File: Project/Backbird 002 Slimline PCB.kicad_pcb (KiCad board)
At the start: 2 copper layers, 10 parts

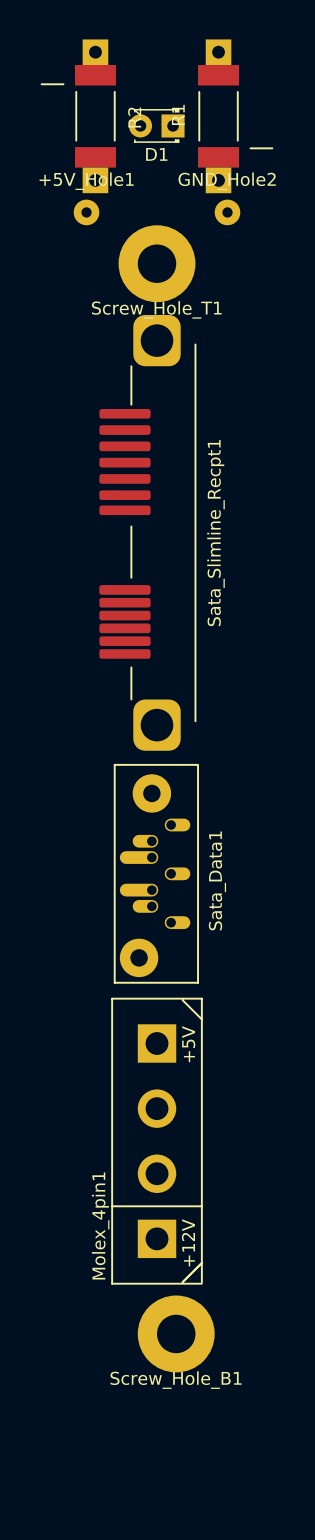
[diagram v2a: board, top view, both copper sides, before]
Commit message: Fixed Sata Slimline footprint to have pads instead of holes. Moved Sata receptacle to the back side of the PCB
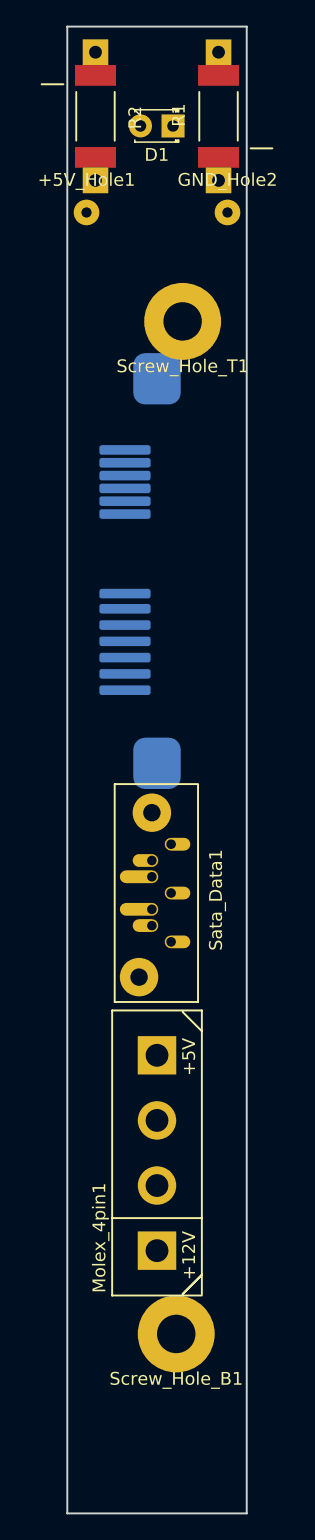
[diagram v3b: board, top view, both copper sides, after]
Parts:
- Sata_Slimline_Recpt1: moved to B.Cu
- moved Screw_Hole_T1 4.92 mm to (109.3, 53.5)
- moved Sata_Slimline_Recpt1 2.98 mm to (107.3, 73.0), turned to 270 degrees
- moved Sata_Data1 1.50 mm to (111.3, 106.5)
- moved Molex_4pin1 0.92 mm to (107.3, 118.4)
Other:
- board outline added: 14 x 116 mm
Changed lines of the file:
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@@
   (general
     (thickness 1.6)
-    (drawings 8)
+    (drawings 14)
     (tracks 0)
     (zones 0)
@@
     (add_net "Net-(Screw_Hole_T1-Pad1)")
   )
+  (module ProjectFootprints:SATA_SLIMLINE_RECPT_1735539-2 (layer B.Cu)
+    (at 107.3 72.96 270)
+    (attr smd)
+    (fp_text reference Sata_Slimline_Recpt1 (at 0 -4.5 270) (layer B.SilkS)
+      (effects (font (size 1 1) (thickness 0.15)) (justify mirror))
+    )
+    (fp_text value Conn_01x13 (at 0 8.08 270) (layer B.Fab)
+      (effects (font (size 1 1) (thickness 0.15)) (justify mirror))
+    )
+    (fp_line (start 10 2) (end 13 2) (layer B.SilkS) (width 0.15))
+    (fp_line (start -13 2) (end -10.5 2) (layer B.SilkS) (width 0.15))
+    (fp_line (start -3.5 2) (end 0.5 2) (layer B.SilkS) (width 0.15))
+    (fp_line (start 14.7 -3) (end -14.7 -3) (layer B.SilkS) (width 0.15))
+    (pad "" smd roundrect (at 15 0 270) (size 4 3.7) (layers B.Cu B.Paste B.Mask) (roundrect_rratio 0.25))
+    (pad "" smd roundrect (at -15 0 270) (size 4 3.7) (layers B.Cu B.Paste B.Mask) (roundrect_rratio 0.25))
+    (pad 7 smd roundrect (at 1.76 2.5 270) (size 0.75 4) (layers B.Cu B.Paste B.Mask) (roundrect_rratio 0.25)
+      (net 2 GND))
+    (pad 6 smd roundrect (at 2.94 2.5 270) (size 0.75 4) (layers B.Cu B.Paste B.Mask) (roundrect_rratio 0.25)
+      (net 5 B+))
+    (pad 5 smd roundrect (at 4.21 2.5 270) (size 0.75 4) (layers B.Cu B.Paste B.Mask) (roundrect_rratio 0.25)
+      (net 6 B-))
+    (pad 4 smd roundrect (at 5.48 2.5 270) (size 0.75 4) (layers B.Cu B.Paste B.Mask) (roundrect_rratio 0.25)
+      (net 2 GND))
+    (pad 3 smd roundrect (at 6.75 2.5 270) (size 0.75 4) (layers B.Cu B.Paste B.Mask) (roundrect_rratio 0.25)
+      (net 7 A-))
+    (pad 2 smd roundrect (at 8.02 2.5 270) (size 0.75 4) (layers B.Cu B.Paste B.Mask) (roundrect_rratio 0.25)
+      (net 8 A+))
+    (pad 1 smd roundrect (at 9.29 2.5 270) (size 0.75 4) (layers B.Cu B.Paste B.Mask) (roundrect_rratio 0.25)
+      (net 2 GND))
+    (pad 8 smd roundrect (at -4.45 2.5 270) (size 0.75 4) (layers B.Cu B.Paste B.Mask) (roundrect_rratio 0.25)
+      (net 10 "Net-(Sata_Slimline_Recpt1-Pad8)"))
+    (pad 9 smd roundrect (at -5.45 2.5 270) (size 0.75 4) (layers B.Cu B.Paste B.Mask) (roundrect_rratio 0.25)
+      (net 3 +5V))
+    (pad 10 smd roundrect (at -6.45 2.5 270) (size 0.75 4) (layers B.Cu B.Paste B.Mask) (roundrect_rratio 0.25)
+      (net 3 +5V))
+    (pad 11 smd roundrect (at -7.45 2.5 270) (size 0.75 4) (layers B.Cu B.Paste B.Mask) (roundrect_rratio 0.25)
+      (net 9 "Net-(Sata_Slimline_Recpt1-Pad11)"))
+    (pad 12 smd roundrect (at -8.45 2.5 270) (size 0.75 4) (layers B.Cu B.Paste B.Mask) (roundrect_rratio 0.25)
+      (net 2 GND))
+    (pad 13 smd roundrect (at -9.45 2.5 270) (size 0.75 4) (layers B.Cu B.Paste B.Mask) (roundrect_rratio 0.25)
+      (net 2 GND))
+  )
   (module Resistors_Universal:Resistor_SMD+THTuniversal_2512_RM10_HandSoldering (layer F.Cu)
     (at 102.5 37.4788 270)
@@
   )
   (module ProjectFootprints:SATA_DATA_678007005_CustomPad (layer F.Cu)
-    (at 111.3 104.98 90)
+    (at 111.3 106.48 90)
     (fp_text reference Sata_Data1 (at 7.86 0.6 90) (layer F.SilkS)
       (effects (font (size 1 1) (thickness 0.15)))
@@
   )
   (module ProjectFootprints:MOLEX_8981_0015244745 (layer F.Cu)
-    (at 107.3 117.44 90)
+    (at 107.3 118.36 90)
     (fp_text reference Molex_4pin1 (at -6.62 -4.5 90) (layer F.SilkS)
       (effects (font (size 1 1) (thickness 0.15)))
@@
       (net 1 "Net-(D1-Pad2)"))
   )
-  (module ProjectFootprints:SATA_SLIMLINE_RECPT_1735539-2 (layer F.Cu)
-    (at 107.3 69.98 90)
-    (attr smd)
-    (fp_text reference Sata_Slimline_Recpt1 (at 0 4.5 90) (layer F.SilkS)
-      (effects (font (size 1 1) (thickness 0.15)))
-    )
-    (fp_text value Conn_01x13 (at 0 -8.08 90) (layer F.Fab)
-      (effects (font (size 1 1) (thickness 0.15)))
-    )
-    (fp_line (start 10 -2) (end 13 -2) (layer F.SilkS) (width 0.15))
-    (fp_line (start -13 -2) (end -10.5 -2) (layer F.SilkS) (width 0.15))
-    (fp_line (start -3.5 -2) (end 0.5 -2) (layer F.SilkS) (width 0.15))
-    (fp_line (start 14.7 3) (end -14.7 3) (layer F.SilkS) (width 0.15))
-    (pad "" np_thru_hole roundrect (at 15 0 90) (size 4 3.7) (drill 2.54) (layers *.Cu *.Mask) (roundrect_rratio 0.25))
-    (pad "" np_thru_hole roundrect (at -15 0 90) (size 4 3.7) (drill 2.54) (layers *.Cu *.Mask) (roundrect_rratio 0.25))
-    (pad 7 smd roundrect (at 1.76 -2.5 90) (size 0.75 4) (layers F.Cu F.Paste F.Mask) (roundrect_rratio 0.25)
-      (net 2 GND))
-    (pad 6 smd roundrect (at 2.94 -2.5 90) (size 0.75 4) (layers F.Cu F.Paste F.Mask) (roundrect_rratio 0.25)
-      (net 5 B+))
-    (pad 5 smd roundrect (at 4.21 -2.5 90) (size 0.75 4) (layers F.Cu F.Paste F.Mask) (roundrect_rratio 0.25)
-      (net 6 B-))
-    (pad 4 smd roundrect (at 5.48 -2.5 90) (size 0.75 4) (layers F.Cu F.Paste F.Mask) (roundrect_rratio 0.25)
-      (net 2 GND))
-    (pad 3 smd roundrect (at 6.75 -2.5 90) (size 0.75 4) (layers F.Cu F.Paste F.Mask) (roundrect_rratio 0.25)
-      (net 7 A-))
-    (pad 2 smd roundrect (at 8.02 -2.5 90) (size 0.75 4) (layers F.Cu F.Paste F.Mask) (roundrect_rratio 0.25)
-      (net 8 A+))
-    (pad 1 smd roundrect (at 9.29 -2.5 90) (size 0.75 4) (layers F.Cu F.Paste F.Mask) (roundrect_rratio 0.25)
-      (net 2 GND))
-    (pad 8 smd roundrect (at -4.45 -2.5 90) (size 0.75 4) (layers F.Cu F.Paste F.Mask) (roundrect_rratio 0.25)
-      (net 10 "Net-(Sata_Slimline_Recpt1-Pad8)"))
-    (pad 9 smd roundrect (at -5.45 -2.5 90) (size 0.75 4) (layers F.Cu F.Paste F.Mask) (roundrect_rratio 0.25)
-      (net 3 +5V))
-    (pad 10 smd roundrect (at -6.45 -2.5 90) (size 0.75 4) (layers F.Cu F.Paste F.Mask) (roundrect_rratio 0.25)
-      (net 3 +5V))
-    (pad 11 smd roundrect (at -7.45 -2.5 90) (size 0.75 4) (layers F.Cu F.Paste F.Mask) (roundrect_rratio 0.25)
-      (net 9 "Net-(Sata_Slimline_Recpt1-Pad11)"))
-    (pad 12 smd roundrect (at -8.45 -2.5 90) (size 0.75 4) (layers F.Cu F.Paste F.Mask) (roundrect_rratio 0.25)
-      (net 2 GND))
-    (pad 13 smd roundrect (at -9.45 -2.5 90) (size 0.75 4) (layers F.Cu F.Paste F.Mask) (roundrect_rratio 0.25)
-      (net 2 GND))
-  )
   (module ProjectFootprints:Blackbird002_Slimline_PCB_Screw (layer F.Cu)
     (at 108.8 132.48)
@@
   )
   (module ProjectFootprints:Blackbird002_Slimline_PCB_Screw (layer F.Cu)
-    (at 107.3 48.98)
+    (at 109.3 53.48)
     (fp_text reference Screw_Hole_T1 (at 0 3.5) (layer F.SilkS)
       (effects (font (size 1 1) (thickness 0.15)))
@@
     (pad 1 thru_hole circle (at 0 0) (size 1.99898 1.99898) (drill 0.8001) (layers *.Cu *.Mask)
       (net 2 GND))
+  )
+  (gr_line (start 114.3 30.48) (end 114.3 146.48) (layer Edge.Cuts) (width 0.15))
+  (gr_line (start 100.3 30.48) (end 114.3 30.48) (layer Edge.Cuts) (width 0.15))
+  (gr_line (start 100.3 146.48) (end 100.3 30.48) (layer Edge.Cuts) (width 0.15))
+  (gr_line (start 114.3 146.48) (end 100.3 146.48) (layer Edge.Cuts) (width 0.15))
+  (dimension 4 (width 0.3) (layer F.SilkS)
+    (gr_text "4.000 mm" (at 112.3 25.38) (layer F.SilkS)
+      (effects (font (size 1.5 1.5) (thickness 0.3)))
+    )
+    (feature1 (pts (xy 110.3 28.98) (xy 110.3 26.893579)))
+    (feature2 (pts (xy 114.3 28.98) (xy 114.3 26.893579)))
+    (crossbar (pts (xy 114.3 27.48) (xy 110.3 27.48)))
+    (arrow1a (pts (xy 110.3 27.48) (xy 111.426504 26.893579)))
+    (arrow1b (pts (xy 110.3 27.48) (xy 111.426504 28.066421)))
+    (arrow2a (pts (xy 114.3 27.48) (xy 113.173496 26.893579)))
+    (arrow2b (pts (xy 114.3 27.48) (xy 113.173496 28.066421)))
+  )
+  (dimension 24.5 (width 0.3) (layer F.SilkS)
+    (gr_text "24.500 mm" (at 124.4 42.73 270) (layer F.SilkS)
+      (effects (font (size 1.5 1.5) (thickness 0.3)))
+    )
+    (feature1 (pts (xy 119.3 54.98) (xy 122.886421 54.98)))
+    (feature2 (pts (xy 119.3 30.48) (xy 122.886421 30.48)))
+    (crossbar (pts (xy 122.3 30.48) (xy 122.3 54.98)))
+    (arrow1a (pts (xy 122.3 54.98) (xy 121.713579 53.853496)))
+    (arrow1b (pts (xy 122.3 54.98) (xy 122.886421 53.853496)))
+    (arrow2a (pts (xy 122.3 30.48) (xy 121.713579 31.606504)))
+    (arrow2b (pts (xy 122.3 30.48) (xy 122.886421 31.606504)))
   )
   (dimension 8 (width 0.3) (layer Eco1.User)
@@
   )
   (dimension 116 (width 0.3) (layer Eco1.User)
-    (gr_text "116.000 mm" (at 126.4 88.48 270) (layer Eco1.User)
-      (effects (font (size 1.5 1.5) (thickness 0.3)))
-    )
-    (feature1 (pts (xy 119.3 146.48) (xy 124.886421 146.48)))
-    (feature2 (pts (xy 119.3 30.48) (xy 124.886421 30.48)))
-    (crossbar (pts (xy 124.3 30.48) (xy 124.3 146.48)))
-    (arrow1a (pts (xy 124.3 146.48) (xy 123.713579 145.353496)))
-    (arrow1b (pts (xy 124.3 146.48) (xy 124.886421 145.353496)))
-    (arrow2a (pts (xy 124.3 30.48) (xy 123.713579 31.606504)))
-    (arrow2b (pts (xy 124.3 30.48) (xy 124.886421 31.606504)))
+    (gr_text "116.000 mm" (at 131.4 88.48 270) (layer Eco1.User)
+      (effects (font (size 1.5 1.5) (thickness 0.3)))
+    )
+    (feature1 (pts (xy 124.3 146.48) (xy 129.886421 146.48)))
+    (feature2 (pts (xy 124.3 30.48) (xy 129.886421 30.48)))
+    (crossbar (pts (xy 129.3 30.48) (xy 129.3 146.48)))
+    (arrow1a (pts (xy 129.3 146.48) (xy 128.713579 145.353496)))
+    (arrow1b (pts (xy 129.3 146.48) (xy 129.886421 145.353496)))
+    (arrow2a (pts (xy 129.3 30.48) (xy 128.713579 31.606504)))
+    (arrow2b (pts (xy 129.3 30.48) (xy 129.886421 31.606504)))
   )
   (gr_line (start 114.3 30.48) (end 114.3 146.48) (layer Eco1.User) (width 0.2))

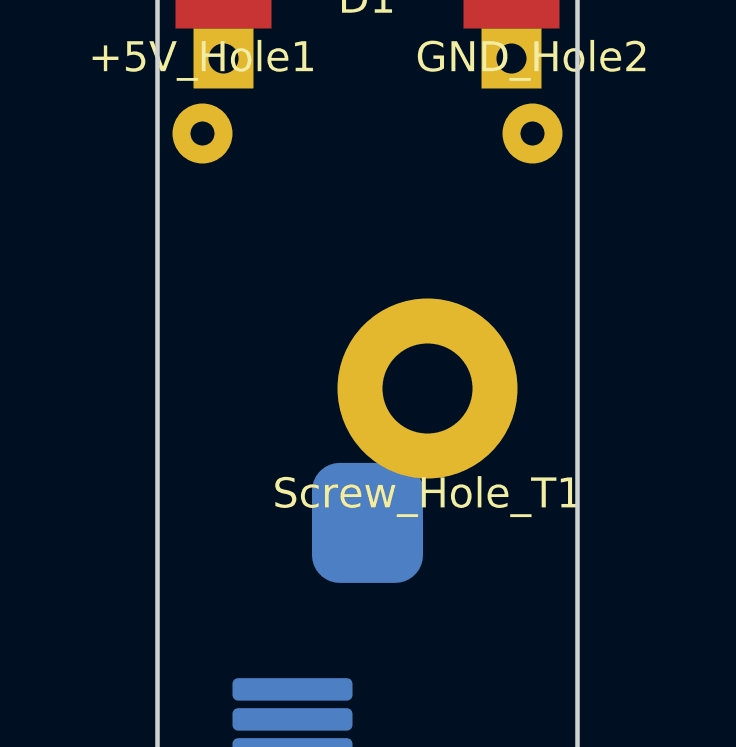
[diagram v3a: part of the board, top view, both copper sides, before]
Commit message: Added elongated screw hole
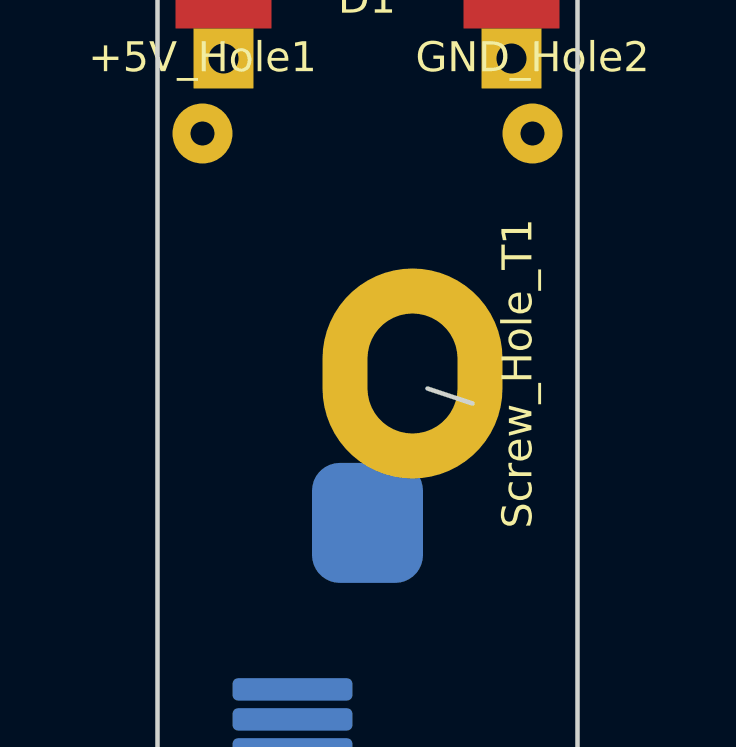
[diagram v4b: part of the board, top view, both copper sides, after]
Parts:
- Screw_Hole_T1: footprint ProjectFootprints:Blackbird002_Slimline_PCB_Screw -> ProjectFootprints:Blackbird002_Slimline_PCB_Screw_Long
- moved Screw_Hole_T1 0.71 mm to (108.8, 53.0), turned to 90 degrees
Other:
- outline, holes or cut-outs redrawn
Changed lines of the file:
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@@
   (general
     (thickness 1.6)
-    (drawings 14)
+    (drawings 15)
     (tracks 0)
     (zones 0)
@@
       (net 11 "Net-(Screw_Hole_B1-Pad1)"))
   )
-  (module ProjectFootprints:Blackbird002_Slimline_PCB_Screw (layer F.Cu)
-    (at 109.3 53.48)
-    (fp_text reference Screw_Hole_T1 (at 0 3.5) (layer F.SilkS)
-      (effects (font (size 1 1) (thickness 0.15)))
-    )
-    (fp_text value Conn_01x01 (at 0 -3.5) (layer F.Fab)
-      (effects (font (size 1 1) (thickness 0.15)))
-    )
-    (pad 1 thru_hole circle (at 0 0) (size 6 6) (drill 3) (layers *.Cu *.Mask)
-      (net 12 "Net-(Screw_Hole_T1-Pad1)"))
-  )
   (module Wire_Pads:SolderWirePad_single_0-8mmDrill (layer F.Cu)
     (at 101.8 44.98)
@@
       (net 2 GND))
   )
+  (module ProjectFootprints:Blackbird002_Slimline_PCB_Screw_Long (layer F.Cu)
+    (at 108.8 52.98 90)
+    (fp_text reference Screw_Hole_T1 (at 0 3.5 90) (layer F.SilkS)
+      (effects (font (size 1 1) (thickness 0.15)))
+    )
+    (fp_text value Conn_01x01 (at 0 -3.5 90) (layer F.Fab)
+      (effects (font (size 1 1) (thickness 0.15)))
+    )
+    (pad 1 thru_hole oval (at 0 0 90) (size 7 6) (drill oval 4 3) (layers *.Cu *.Mask)
+      (net 12 "Net-(Screw_Hole_T1-Pad1)"))
+  )
+  (gr_line (start 109.3 53.48) (end 110.8 53.98) (layer Edge.Cuts) (width 0.15))
   (gr_line (start 114.3 30.48) (end 114.3 146.48) (layer Edge.Cuts) (width 0.15))
   (gr_line (start 100.3 30.48) (end 114.3 30.48) (layer Edge.Cuts) (width 0.15))

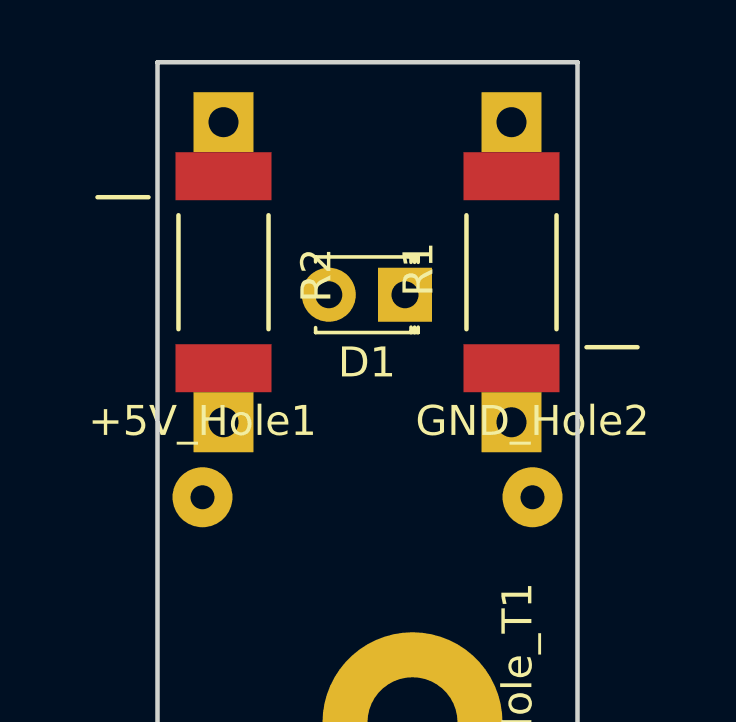
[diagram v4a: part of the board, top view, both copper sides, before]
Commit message: Moved LED and resistors to the back side of the PCB
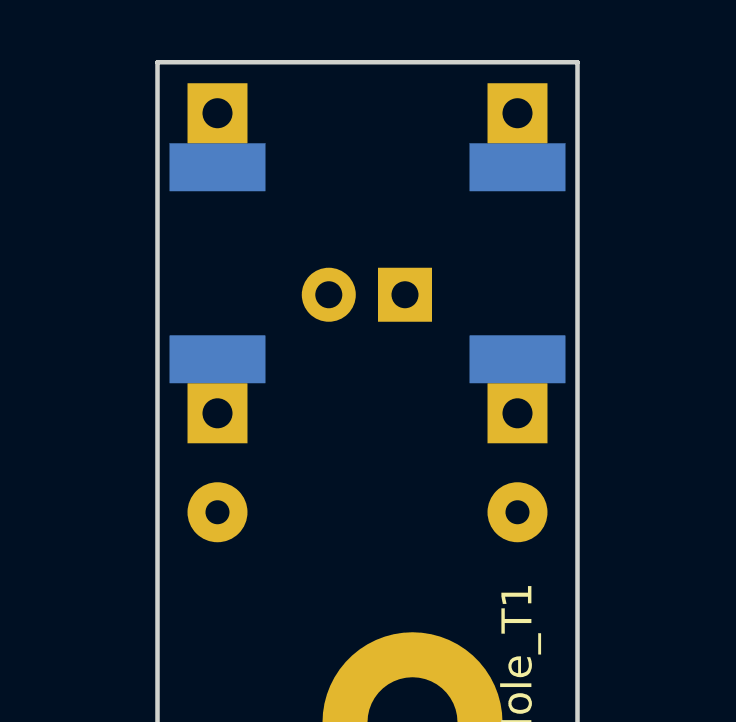
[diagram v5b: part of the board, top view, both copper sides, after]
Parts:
- +5V_Hole1, D1, GND_Hole2, R1, R2: moved to B.Cu
- moved +5V_Hole1 0.71 mm to (102.3, 45.5)
- moved GND_Hole2 0.71 mm to (112.3, 45.5)
- moved R1 0.36 mm to (112.3, 37.2)
- moved R2 0.36 mm to (102.3, 37.2)

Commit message: Moved silk screen of resistors and LED power holes to be on the PCB.
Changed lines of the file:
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@@
     (descr "Resistor, SMD+THT, 2512, RM10, Hand soldering,")
     (tags "Resistor, SMD+THT, 2512, RM10, Hand soldering,")
-    (fp_text reference R2 (at 0.09906 3.0988 270) (layer B.SilkS)
+    (fp_text reference R2 (at -5.2004 -2.5 270) (layer B.SilkS)
       (effects (font (size 1 1) (thickness 0.15)) (justify mirror))
     )
@@
     (descr "Resistor, SMD+THT, 2512, RM10, Hand soldering,")
     (tags "Resistor, SMD+THT, 2512, RM10, Hand soldering,")
-    (fp_text reference R1 (at 0.09906 3.0988 90) (layer B.SilkS)
+    (fp_text reference R1 (at 5.2004 -2.5 90) (layer B.SilkS)
       (effects (font (size 1 1) (thickness 0.15)) (justify mirror))
     )
@@
   (module Wire_Pads:SolderWirePad_single_0-8mmDrill (layer B.Cu)
     (at 102.3 45.48)
-    (fp_text reference +5V_Hole1 (at 0 2.54) (layer B.SilkS)
+    (fp_text reference +5V_Hole1 (at -1 5 90) (layer B.SilkS)
       (effects (font (size 1 1) (thickness 0.15)) (justify mirror))
     )
@@
   (module Wire_Pads:SolderWirePad_single_0-8mmDrill (layer B.Cu)
     (at 112.3 45.48)
-    (fp_text reference GND_Hole2 (at 0 2.54) (layer B.SilkS)
+    (fp_text reference GND_Hole2 (at 1 5.5 90) (layer B.SilkS)
       (effects (font (size 1 1) (thickness 0.15)) (justify mirror))
     )
@@
   (module ProjectFootprints:Blackbird002_Slimline_PCB_Screw_Long (layer F.Cu)
     (at 108.8 52.98 90)
-    (fp_text reference Screw_Hole_T1 (at 0 3.5 90) (layer F.SilkS)
+    (fp_text reference Screw_Hole_T1 (at 0 4 90) (layer F.SilkS)
       (effects (font (size 1 1) (thickness 0.15)))
     )

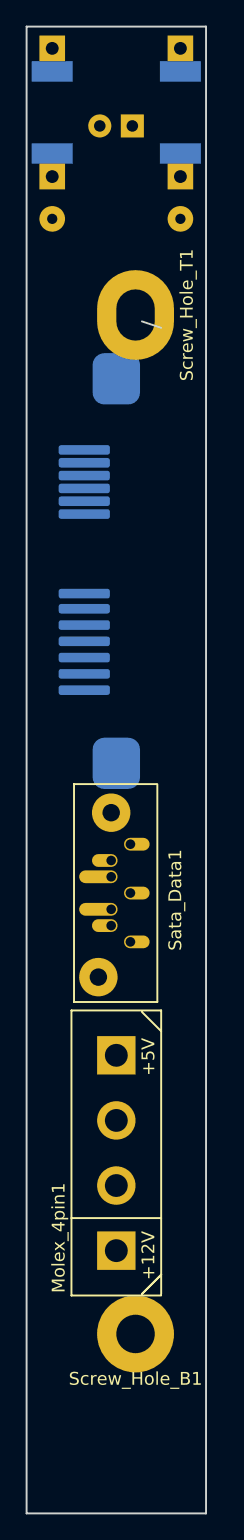
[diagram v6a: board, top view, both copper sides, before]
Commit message: Moved top drill hole and Sata Recpt into the correct positions. Edited the pads on the Sata Recpt footprint to be more accurate. Still need to add traces
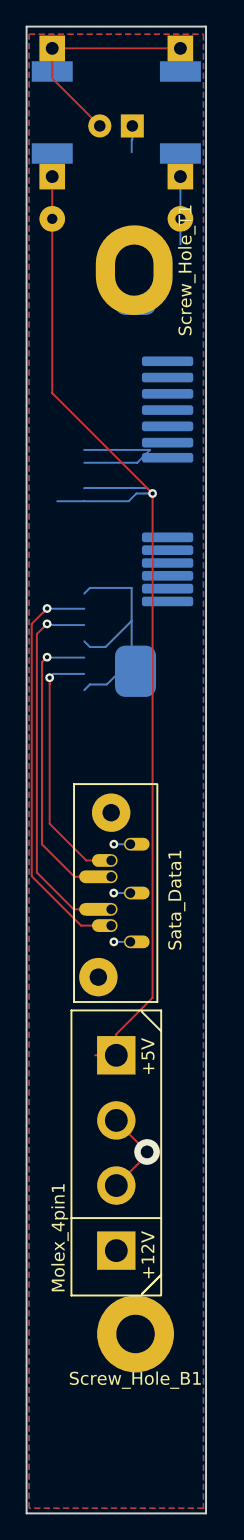
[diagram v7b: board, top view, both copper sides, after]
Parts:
- moved Sata_Slimline_Recpt1 7.24 mm to (108.8, 65.9), turned to 90 degrees
- moved Screw_Hole_T1 3.50 mm to (108.7, 49.5)
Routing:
- net +5V: track 0.00 -> 87.8 mm, vias 0 -> 1
- net B+: track 0.00 -> 32.1 mm, vias 0 -> 1
- net GND: track 0.00 -> 31.5 mm, vias 0 -> 4
- net B-: track 0.00 -> 30.3 mm, vias 0 -> 1
- net A-: track 0.00 -> 24.1 mm, vias 0 -> 1
- net A+: track 0.00 -> 20.2 mm, vias 0 -> 1
- net (no net): track 0.00 -> 18.9 mm
- net Net-(D1-Pad2): track 0.00 -> 17.6 mm
- added copper zone on F.Cu, net +5V
- added copper zone on B.Cu, net GND
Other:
- outline, holes or cut-outs redrawn
